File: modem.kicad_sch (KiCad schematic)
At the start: 10 parts, among them J1 2337019-1, U2 EG800QEULC-N03-SNNSA

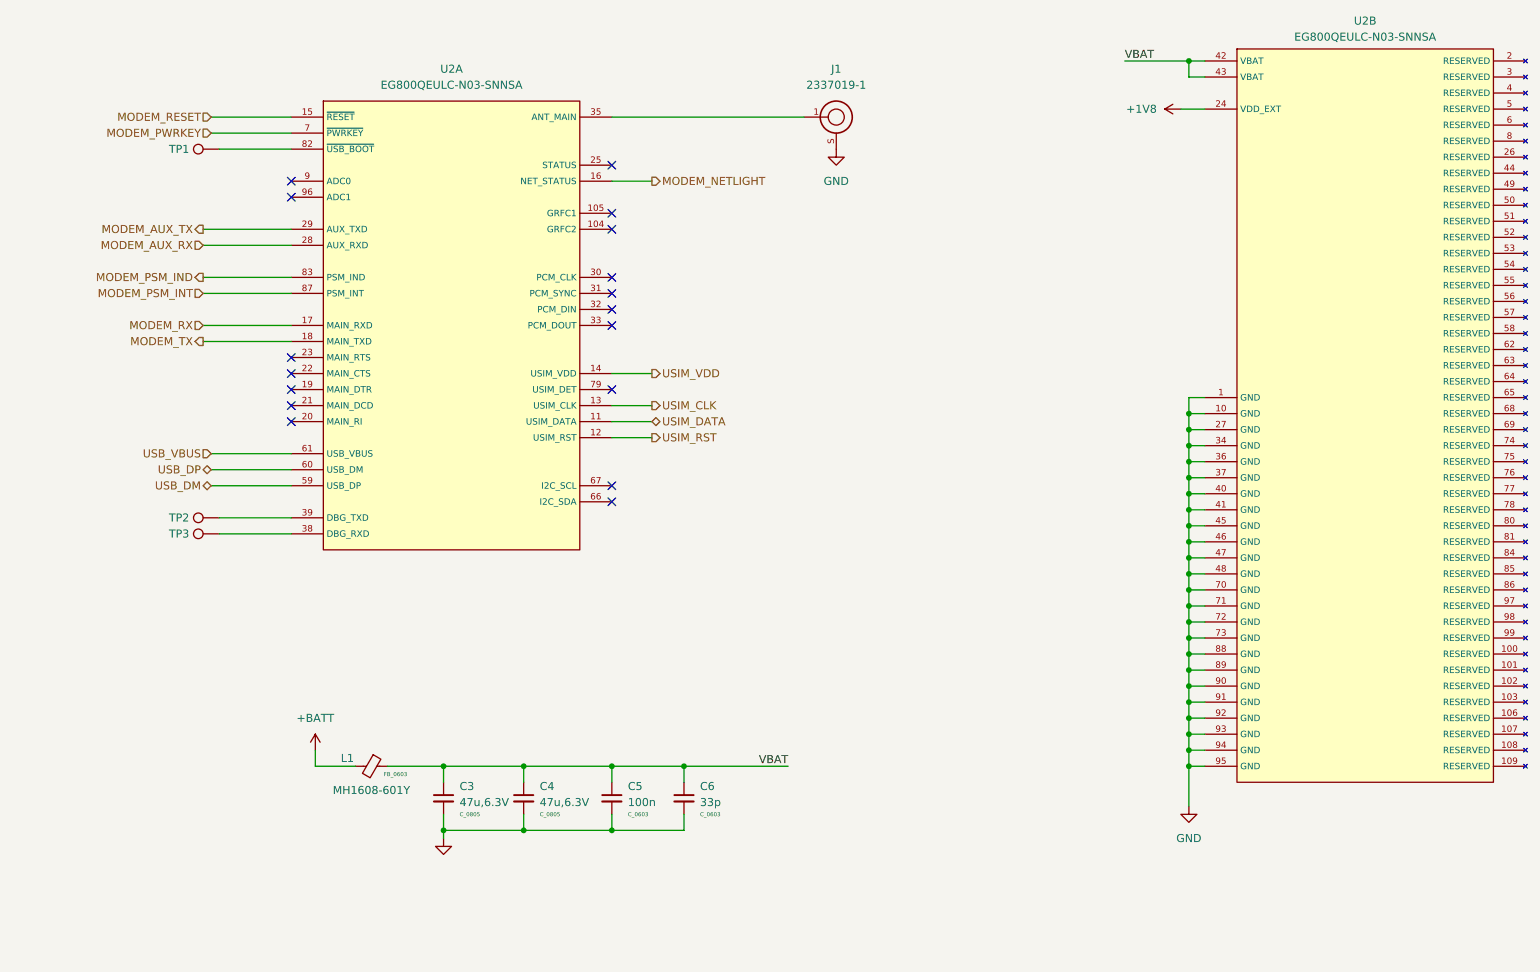
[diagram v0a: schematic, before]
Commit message: Add test points. Finish layout
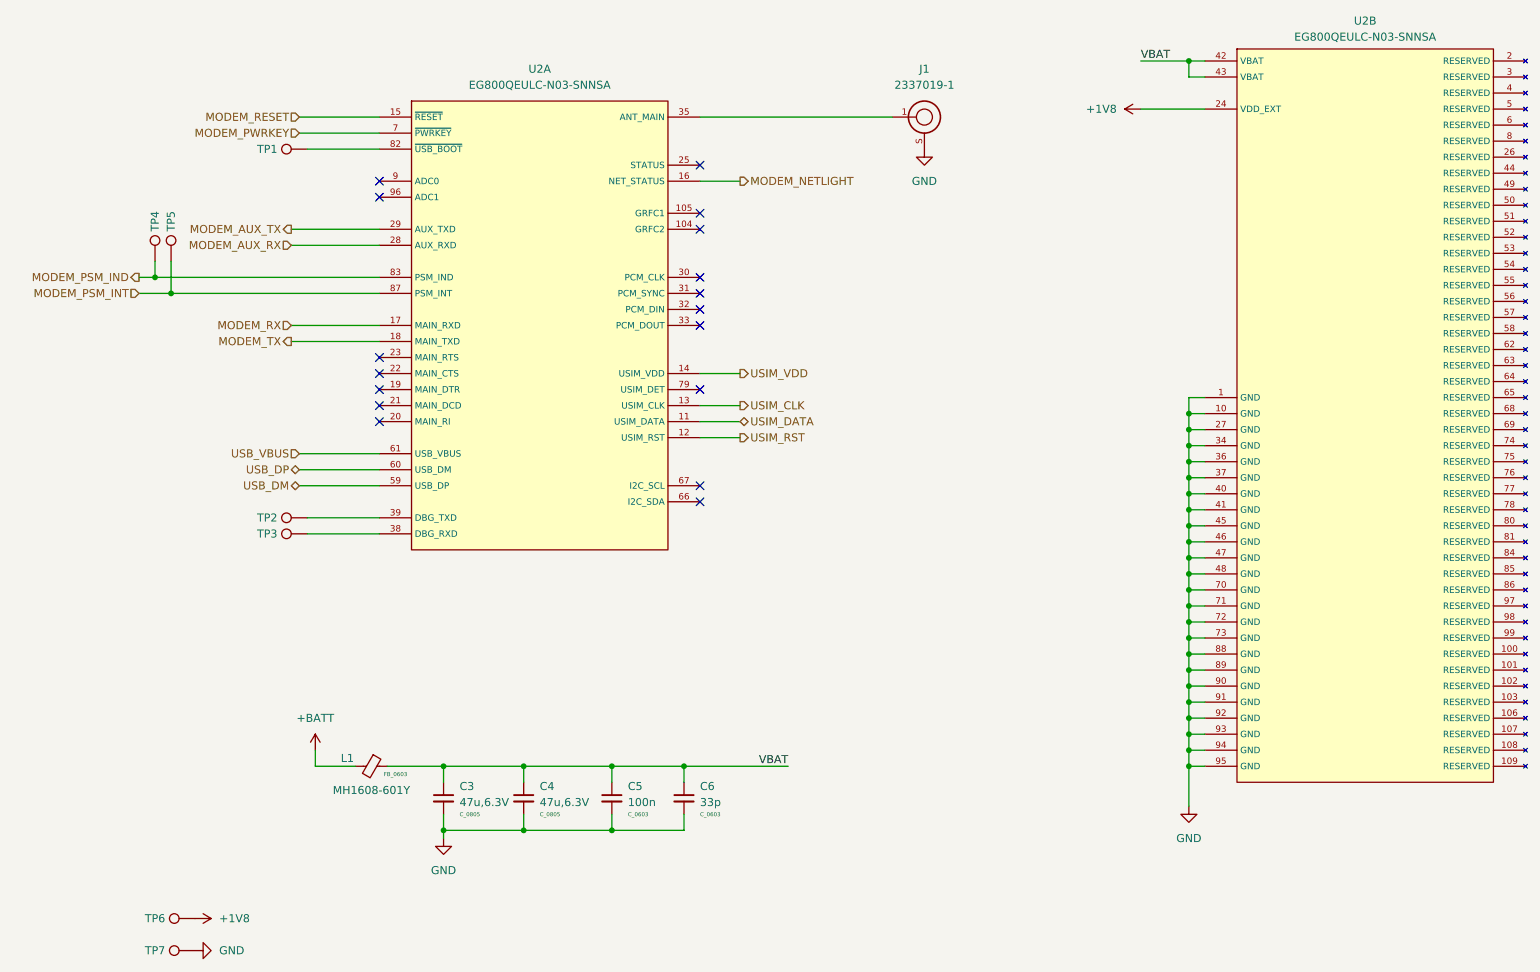
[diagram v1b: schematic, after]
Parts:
- added TP4, TP5, TP6, TP7: ~, TP_TestPoint:TestPoint_1mm, symbol TP_TestPoint:TestPoint_1mm
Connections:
- net +1V8: now also TP6.1
- net GND: now also TP7.1
- net MODEM_PSM_IND: now also TP4.1
- net MODEM_PSM_INT: now also TP5.1
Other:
- moved on the sheet: J1, TP1, TP2, TP3, U2A
